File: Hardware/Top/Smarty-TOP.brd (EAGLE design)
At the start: 38 x 38 mm, 52 parts, among them SW6 SWITCH.MOM, SW7 SWITCH.MOM, SW8 SWITCH.MOM, U2 NRF52832_MODULE_MDBT42, U4 PCF8523

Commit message: Take 001 and part of Take 002 Completed
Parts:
- removed C10, C11: 300p, LinnesLab-Passives:C0603
- removed C12: 10u, LinnesLab-Passives:C0805
- removed C14: 100n, LinnesLab-Passives:C0603
- removed CORTEX1: CORTEX_DEBUG_PTH, LinnesLab-Connectors:2X5-PTH-1.27MM
- removed D1: (no value), LinnesLab-DiscreteSemi:USC
- removed L2: 10u, LinnesLab-Passives:L0603
- removed R8, R9: 10k, LinnesLab-Passives:R0603
- removed SW3, SW4: (no value), LinnesLab-Switches:BUTTON-GULLWING
- removed XTAL2: 32.768kHz, LinnesLab-Clocks:2-SMD.NOLEAD.2.0MMTO1.2MM
- added C26: 1u, LinnesLab-Passives:C0603
- added C27, C28: (no value), LinnesLab-Passives:C0603
- added C29, C30: 300p, LinnesLab-Passives:C0603
- added C31: 10u, LinnesLab-Passives:C0805
- added C32: 100n, LinnesLab-Passives:C0603
- added CORTEX3: CORTEX_DEBUG_PTH, LinnesLab-Connectors:2X5-PTH-1.27MM
- added D3: (no value), LinnesLab-DiscreteSemi:USC
- added JP2: (no value), LinnesLab-Switches:SMT-JUMPER_2_NO_SILK
- added L3: 10u, LinnesLab-Passives:L0603
- added LED5: RED, LinnesLab-LED:LED-0603
- added LED6: BLUE, LinnesLab-LED:LED-0603
- added R1, R2: 0, LinnesLab-Passives:R0603
- added R10: 27, LinnesLab-Passives:R0603
- added R16, R17, R19, R20: 1k, LinnesLab-Passives:R0603
- added R18: 10k, LinnesLab-Passives:R0603
- added SW1: SWITCH.MOM, LinnesLab-Switches:TACTILE_SWITCH_SMD_6.2MM_TALL
- added U5: NRF52832_MODULE_MDBT42, LinnesLab-Microcontrollers:BLE_MODULE_RAYTAC_MDBT42
- added XTAL4: 32.768kHz, LinnesLab-Clocks:2-SMD.NOLEAD.2.0MMTO1.2MM
- C7: value 1u -> 100n
- C8, C9: value (none) -> 47p
- LED4: value BLUE -> YELLOW
- R3, R4: value 1k -> 10k
- R5: value 10k -> 27
- SW7, SW8: value SWITCH.MOM -> (none); device LinnesLab-Switches:TACTILE_SWITCH_SMD_6.2MM_TALL -> LinnesLab-Switches:BUTTON-GULLWING
- U2: value NRF52832_MODULE_MDBT42 -> FT231XS; device LinnesLab-Microcontrollers:BLE_MODULE_RAYTAC_MDBT42 -> LinnesLab-DigitalIC:SSOP20_L
- moved SW7 59.6 mm to (75.1, 17.4)
- moved R4 58.9 mm to (-3.73, -11.9), turned to 0 degrees
- moved R3 55.4 mm to (-3.73, -9.22), turned to 0 degrees
- moved C7 42.3 mm to (65.6, 36.0), turned to 0 degrees
- moved C8 42.0 mm to (65.6, 30.9)
- moved SW8 38.7 mm to (68.0, 5.94), turned to 180 degrees
- moved C9 36.7 mm to (65.6, 25.9)
- moved XTAL3 32.6 mm to (7.70, -4.78)
- moved U4 32.4 mm to (12.4, -5.97)
- moved C2 32.1 mm to (14.2, -2.08)
- moved LED3 28.1 mm to (69.4, 35.8)
- moved LED4 26.2 mm to (69.4, 32.0)
- moved SW6 26.0 mm to (32.1, 4.04)
- moved R5 15.9 mm to (52.0, 33.8), turned to 0 degrees
- moved U2 14.0 mm to (18.4, 27.5), turned to 270 degrees
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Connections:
- net VBATT renamed VBAT
- removed net N$10: LED4.A, R4.1
- removed net N$18: SW6.B1, SW6.B2
- removed net N$21: SW7.A1, SW7.A2
- removed net N$22: SW7.B1, SW7.B2
- removed net N$23: SW8.A1, SW8.A2
- removed net N$24: SW8.B1, SW8.B2
- removed net N$4: C8.2, U2.13, XTAL2.P$1
- removed net N$6: C9.1, U2.14, XTAL2.P$2
- removed net N$9: LED3.A, R3.1
- removed net RXD: U2.21
- removed net TXD: U2.19
- new net !CTS: JP2.2, U2.9
- new net FT3V3: U2.13
- new net N$26: C27.2, U5.13, XTAL4.P$1
- new net N$27: C28.1, U5.14, XTAL4.P$2
- new net N$28: LED5.A, R16.1
- new net N$29: LED6.A, R17.1
- new net N$30: L3.1, U5.10
- new net N$31: C26.1, L3.2, U5.9
- new net N$32: CORTEX3.8
- new net RXD.FT: R2.1, U2.4
- new net RXD.NRF: R1.2, U5.21
- new net RXLED: R19.1, U2.17
- new net SW1: SW1.A1, SW6.A1
- new net TXD.FT: R1.1, U2.20
- new net TXD.NRF: R2.2, U5.19
- new net TXLED: R20.1, U2.10
- net 3.3V: now also C31.2, C7.2, CORTEX3.1, D3.-, LED3.A, LED4.A, R18.2, R3.2, R4.2, U2.14, U2.3, U5.11; no longer C12.2, CORTEX1.1, D1.-, R5.2, R8.2, R9.2, U2.11
- net DFU: now also SW7.3, U5.34; no longer SW3.3, U2.34
- net DTR: now also C32.1, U2.1; no longer C14.1
- net FRST: now also U5.38; no longer U2.38
- net GND: now also C26.2, C27.1, C28.2, C29.2, C30.2, C31.1, C7.1, C8.2, C9.1, CORTEX3.3, CORTEX3.5, CORTEX3.7, CORTEX3.9, JP2.1, LED5.C, LED6.C, SW1.B1, SW1.B2, SW6.B1, SW6.B2, SW7.1, SW8.3, U2.16, U2.6, U5.1, U5.12, U5.24, U5.39, USB2.S1, USB2.S2, USB2.S3, USB2.S4, USB2.S5, USB2.S6; no longer C10.2, C11.2, C12.1, C7.2, C8.1, C9.2, CORTEX1.3, CORTEX1.5, CORTEX1.7, CORTEX1.9, LED3.C, LED4.C, SW3.1, SW4.3, U2.1, U2.12, U2.24, U2.39
- net LED1: now also R16.2, U5.31; no longer R3.2, U2.31
- net LED2: now also R17.2, U5.33; no longer R4.2, U2.33
- net MISO: now also U5.28; no longer U2.28
- net MOSI: now also U5.27; no longer U2.27
- net N$11: now also R5.2, U2.12; no longer L2.1, U2.10
- net N$12: now also R10.2, U2.11; no longer C7.1, L2.2, U2.9
- net N$14: now also LED3.C, R19.2; no longer CORTEX1.8
- net N$16: now also LED4.C, R20.2; no longer SW6.A1, SW6.A2
- net P0.09/NFC1: now also C30.1, U5.22; no longer C11.1, U2.22
- net P0.10/NFC2: now also C29.1, U5.23; no longer C10.1, U2.23
- net RESET: now also C32.2, CORTEX3.10, D3.+, R18.1, SW8.1, U5.35; no longer C14.2, CORTEX1.10, D1.+, R5.1, SW4.1, U2.35
- net SCK: now also U5.26; no longer U2.26
- net SCL: now also R4.1, U5.3; no longer R8.1, U2.3
- net SDA: now also R3.1, U5.2; no longer R9.1, U2.2
- net SWCLK: now also CORTEX3.4, U5.36; no longer CORTEX1.4, U2.36
- net SWDIO: now also CORTEX3.2, U5.37; no longer CORTEX1.2, U2.37
- net SWO: now also CORTEX3.6, U5.32; no longer CORTEX1.6, U2.32
- net USB+: now also C8.1, R10.1
- net USB-: now also C9.2, R5.1
- net V_USB: now also U2.15

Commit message: Finished Take 2
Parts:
- removed SW6: SWITCH.MOM, LinnesLab-Switches:TACTILE_SWITCH_SMD_6.2MM_TALL
- added J1: (no value), LinnesLab-Connectors:1X07
- added SW2: SWITCH.MOM, LinnesLab-Switches:TACTILE_SWITCH_SMD_6.2MM_TALL
- moved SW1 10.3 mm to (32.1, 4.04)
- moved U2 0.90 mm to (19.1, 26.8)
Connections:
- removed net BATT: R13.1, R14.2
- removed net CD1: SD2.CD1
- removed net CHRG.STAT: CHRG2.1, R12.1
- removed net CS.OLED: U3.13
- removed net DC.OLED: U3.15
- removed net RESET.OLED: U3.14
- removed net SD.CS: SD2.2
- removed net SW1: SW1.A1, SW6.A1
- new net A4/BATT: R13.1, R14.2, U5.5
- new net A6/TIA: U5.7
- new net A7/PPG: U5.8
- new net D11/SW1: SW1.A1, U5.25
- new net D15/SW2: SW2.A1, U5.29
- new net D16/CS.OLED: U3.13, U5.30
- new net D27/CHRG.STATUS: CHRG2.1, R12.1, U5.4
- new net D29/LED.CTRL: U5.6
- new net D3/RESET.OLED: U3.14, U5.16
- new net D4/DC.OLED: U3.15, U5.17
- new net D5/CD1: SD2.CD1, U5.18
- new net D7/SD.CS: SD2.2, U5.20
- net GND: now also SW2.B1, SW2.B2; no longer SW6.B1, SW6.B2

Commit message: Finished Take 004
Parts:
- removed CHRG2: MCP73831, LinnesLab-Power:SOT23-5
- removed J1: (no value), LinnesLab-Connectors:1X07
- removed LDO2: MIC5504, LinnesLab-Power:SOT23-5
- removed R15: 100k, LinnesLab-Passives:R0603
- added CHRG: MCP73831, LinnesLab-Power:SOT23-5
- added J3: (no value), LinnesLab-Connectors:1X07_1.27MM
- added LDO1: MIC5504, LinnesLab-Power:SOT23-5
- moved R1 84.9 mm to (52.5, 60.1)
- moved R2 83.5 mm to (48.7, 59.9)
- moved U2 40.8 mm to (49.0, 54.6)
- moved R20 36.6 mm to (54.1, 57.6)
- moved C31 32.7 mm to (22.4, 26.3), turned to 270 degrees
- moved R19 31.8 mm to (54.0, 55.9)
- moved C26 30.7 mm to (25.0, 29.0), turned to 90 degrees
- moved C7 29.8 mm to (44.8, 57.5), turned to 270 degrees
- moved R7 28.4 mm to (30.7, 17.4)
- moved LED4 28.1 mm to (57.5, 57.5), turned to 180 degrees
- moved C20 28.1 mm to (18.1, -16.1), turned to 270 degrees
- moved R11 27.8 mm to (16.4, -15.9), turned to 90 degrees
- moved XTAL3 27.3 mm to (34.2, -11.3)
- moved L3 27.2 mm to (25.0, 25.8)
- moved C21 27.2 mm to (9.60, -16.3), turned to 180 degrees
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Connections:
- net 3.3V: now also J3.4, LDO1.5; no longer LDO2.5, R15.2
- net A6/TIA: now also J3.6
- net A7/PPG: now also J3.7
- net D27/CHRG.STATUS: now also CHRG.1; no longer CHRG2.1
- net D29/LED.CTRL: now also J3.5
- net GND: now also CHRG.2, J3.3, LDO1.2; no longer CHRG2.2, LDO2.2, R15.1, SW1.B2, SW2.B2
- net N$17: now also CHRG.5; no longer CHRG2.5
- net SCL: now also J3.2
- net SDA: now also J3.1
- net VIN: now also CHRG.4, LDO1.1, LDO1.3; no longer CHRG2.4, LDO2.1, LDO2.3
- net VLIPO: now also CHRG.3; no longer CHRG2.3
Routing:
- net GND: track 0.00 -> 20.5 mm, vias 0 -> 13
- net TXLED: track 0.00 -> 12.9 mm, vias 0 -> 2
- net VLIPO: track 0.00 -> 12.1 mm
- net VIN: track 0.00 -> 7.85 mm
- net N$2: track 0.00 -> 6.71 mm
- net RXD.FT: track 0.00 -> 5.63 mm
- net N$13: track 0.00 -> 5.40 mm
- net N$8: track 0.00 -> 4.43 mm
- net N$5: track 0.00 -> 4.30 mm
- net 3.3V: track 0.00 -> 3.99 mm, vias 0 -> 1
- net N$31: track 0.00 -> 3.96 mm
- net N$15: track 0.00 -> 3.32 mm
- net !CTS: track 0.00 -> 3.16 mm
- net N$3: track 0.00 -> 2.71 mm
- net N$1: track 0.00 -> 2.70 mm
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- added copper zone on layer 1, net 3.3V
- added copper zone on layer 16, net GND

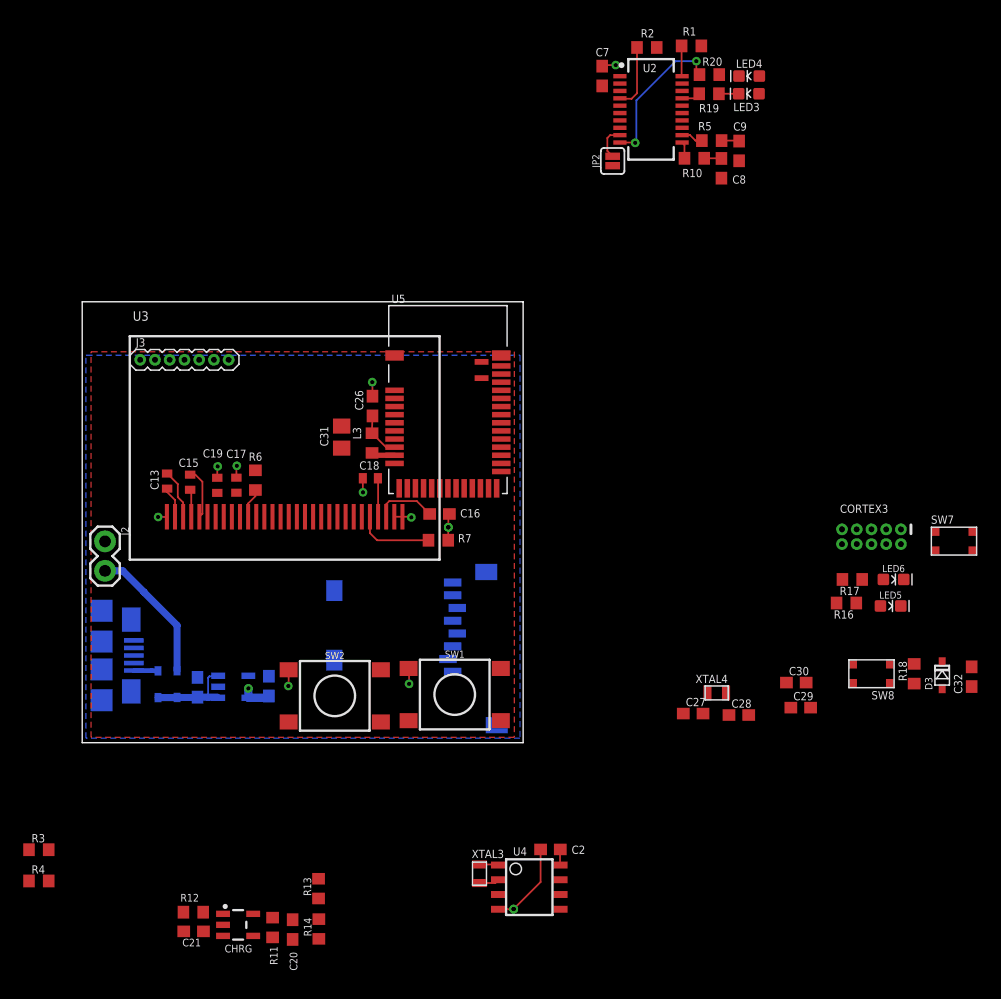
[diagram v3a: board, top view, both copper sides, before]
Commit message: Finished Take 005, Airwire Errors
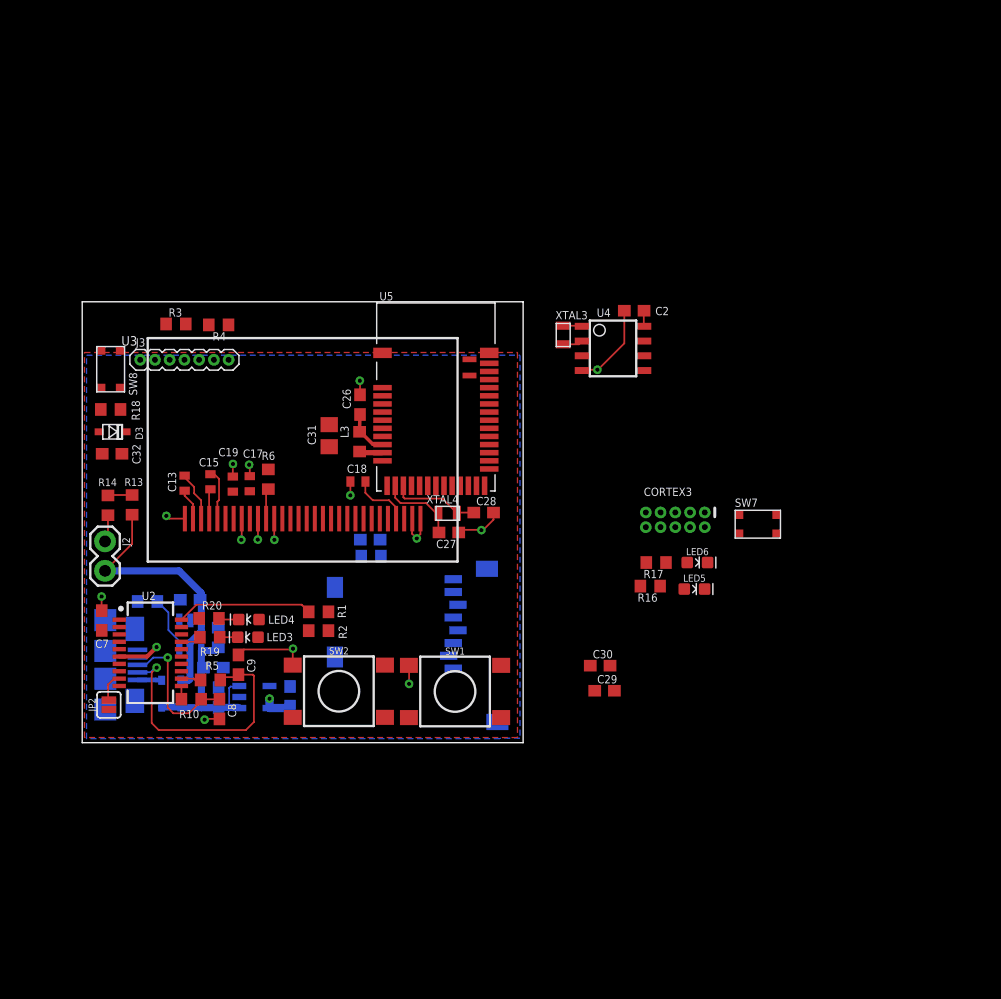
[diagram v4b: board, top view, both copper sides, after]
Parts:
- moved C32 76.5 mm to (2.57, 24.9), turned to 180 degrees
- moved D3 74.5 mm to (2.62, 26.8), turned to 0 degrees
- moved R18 72.9 mm to (2.45, 28.7), turned to 0 degrees
- moved SW8 70.6 mm to (2.45, 32.2), turned to 90 degrees
- moved JP2 63.9 mm to (2.30, 3.27)
- moved C7 63.7 mm to (1.69, 10.5)
- moved LED3 63.7 mm to (14.3, 9.09)
- moved R20 63.7 mm to (10.9, 10.7)
- moved U2 63.7 mm to (5.88, 7.75)
- moved R10 63.7 mm to (9.40, 3.74)
- moved LED4 63.7 mm to (14.4, 10.6)
- moved R19 63.6 mm to (11.0, 9.09)
- moved C8 63.6 mm to (11.8, 2.91)
- moved R5 63.5 mm to (11.0, 5.41)
- moved C9 61.8 mm to (13.5, 6.72), turned to 270 degrees
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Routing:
- net GND: track 20.5 -> 43.5 mm, vias 13 -> 16
- net USB-: track 1.61 -> 23.3 mm, vias 0 -> 1
- net TXLED: track 12.9 -> 0.39 mm, vias 2 -> 0
- net VLIPO: track 12.1 -> 23.6 mm
- net USB+: track 1.49 -> 12.5 mm, vias 0 -> 1
- net TXD.FT: track 2.63 -> 11.8 mm
- net VIN: track 7.85 -> 15.9 mm
- net N$27: track 0.00 -> 7.67 mm
- net N$26: track 0.00 -> 6.98 mm
- net N$2: track 6.71 -> 0.00 mm
- net RXD.FT: track 5.63 -> 0.05 mm
- net N$13: track 5.40 -> 0.00 mm
- net N$17: track 0.00 -> 5.01 mm
- net A4/BATT: track 0.00 -> 2.10 mm
- net N$15: track 3.32 -> 5.15 mm
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
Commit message: Finished Take 006
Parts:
- removed C2, C5, C6: 1u, LinnesLab-Passives:C0603
- removed C20, C21: 4.7u, LinnesLab-Passives:C0603
- removed CHRG: MCP73831, LinnesLab-Power:SOT23-5
- removed LDO1: MIC5504, LinnesLab-Power:SOT23-5
- removed R11: (no value), LinnesLab-Passives:R0603
- removed R12: 100k, LinnesLab-Passives:R0603
- removed SD2: (no value), LinnesLab-Connectors:MICROSD
- removed U4: PCF8523, LinnesLab-Clocks:SO8
- removed XTAL3: 32.7680kHz, LinnesLab-Clocks:2-SMD.NOLEAD.2.0MMTO1.2MM
- moved R18 36.3 mm to (35.0, 12.8), turned to 180 degrees
- moved SW8 36.1 mm to (34.7, 15.9), turned to 270 degrees
- moved C32 36.0 mm to (35.0, 9.38), turned to 0 degrees
- moved D3 35.9 mm to (34.9, 11.1), turned to 180 degrees
- moved SW7 28.7 mm to (35.0, 35.8)
- moved LED5 20.7 mm to (33.5, 20.8), turned to 270 degrees
- moved CORTEX3 19.0 mm to (35.2, 29.5), turned to 270 degrees
- moved R16 18.6 mm to (33.7, 24.0), turned to 90 degrees
- moved LED6 18.3 mm to (35.5, 20.8), turned to 270 degrees
- moved C18 17.2 mm to (41.0, 22.3)
- moved R17 16.4 mm to (35.4, 24.0), turned to 90 degrees
- moved C28 16.1 mm to (18.8, 22.5), turned to 90 degrees
- moved C27 15.1 mm to (17.2, 22.5), turned to 270 degrees
- moved XTAL4 11.3 mm to (20.5, 22.1), turned to 90 degrees
- moved R7 7.55 mm to (31.8, 19.2), flipped to the top, turned to 270 degrees
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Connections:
- removed net CD2: SD2.CD2
- removed net N$17: CHRG.5, R11.2
- removed net N$19: U4.2, XTAL3.P$1
- removed net N$20: U4.1, XTAL3.P$2
- removed net VBAT: U4.3
- net 3.3V: no longer C2.1, C6.1, LDO1.5, SD2.4, U4.8
- net D27/CHRG.STATUS: no longer CHRG.1, R12.1
- net D5/CD1: no longer SD2.CD1
- net D7/SD.CS: no longer SD2.2
- net GND: no longer C2.2, C20.2, C21.1, C5.1, C6.2, CHRG.2, LDO1.2, R11.1, SD2.6, SD2.MT1, SD2.MT2, U4.4
- net MISO: no longer SD2.7
- net MOSI: no longer SD2.3
- net SCK: no longer SD2.5
- net SCL: no longer U4.6
- net SDA: no longer U4.5
- net VIN: no longer C21.2, C5.2, CHRG.4, LDO1.1, LDO1.3, R12.2
- net VLIPO: no longer C20.1, CHRG.3
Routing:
- net RESET: track 0.00 -> 28.5 mm, vias 0 -> 1
- net VIN: track 15.9 -> 1.76 mm
- net SWO: track 0.00 -> 12.0 mm, vias 0 -> 1
- net SWCLK: track 0.00 -> 8.34 mm
- net N$2: track 0.00 -> 7.78 mm
- net LED2: track 0.00 -> 7.66 mm
- net SWDIO: track 0.00 -> 5.53 mm, vias 0 -> 1
- net N$15: track 5.15 -> 0.05 mm
- net N$17: track 5.01 -> 0.00 mm
- net GND: track 43.5 -> 39.0 mm, vias 16 -> 19
- net LED1: track 0.00 -> 4.33 mm
- net N$13: track 0.00 -> 4.27 mm
- net 3.3V: track 3.99 -> 0.11 mm, vias 1 -> 0
- net VLIPO: track 23.6 -> 20.7 mm
- net N$19: track 1.76 -> 0.00 mm
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
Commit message: Almost Done With Take 008
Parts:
- removed C19: 2.2uF, LinnesLab-Passives:C0402
- removed C26: 1u, LinnesLab-Passives:C0603
- removed C27, C28: (no value), LinnesLab-Passives:C0603
- removed C29, C30: 300p, LinnesLab-Passives:C0603
- removed C31: 10u, LinnesLab-Passives:C0805
- removed CORTEX3: CORTEX_DEBUG_PTH, LinnesLab-Connectors:2X5-PTH-1.27MM
- removed L3: 10u, LinnesLab-Passives:L0603
- removed LED5: RED, LinnesLab-LED:LED-0603
- removed LED6: BLUE, LinnesLab-LED:LED-0603
- removed R19, R20: 1k, LinnesLab-Passives:R0603
- removed SW7: (no value), LinnesLab-Switches:BUTTON-GULLWING
- removed XTAL4: 32.768kHz, LinnesLab-Clocks:2-SMD.NOLEAD.2.0MMTO1.2MM
- added C1, C6: 1u, LinnesLab-Passives:C0603
- added C11: 47p, LinnesLab-Passives:C0603
- added C12: 100n, LinnesLab-Passives:C0603
- added C14: 2.2uF, LinnesLab-Passives:C0402
- added C2: 10u, LinnesLab-Passives:C0805
- added C3, C4: (no value), LinnesLab-Passives:C0603
- added C5: 4.7u, LinnesLab-Passives:C0603
- added CHRG1: MCP73831, LinnesLab-Power:SOT23-5
- added DEBUG1: CORTEX_DEBUG_PTH, LinnesLab-Connectors:2X5-PTH-1.27MM
- added L1: 10u, LinnesLab-Passives:L0603
- added LDO1: MIC5504, LinnesLab-Power:SOT23-5
- added LED1: RED, LinnesLab-LED:LED-0603
- added LED2: BLUE, LinnesLab-LED:LED-0603
- added R11: 27, LinnesLab-Passives:R0603
- added R12: 10k, LinnesLab-Passives:R0603
- added R15: 1k, LinnesLab-Passives:R0603
- added R8: 100k, LinnesLab-Passives:R0603
- added SW3: SWITCH.MOM, LinnesLab-Switches:TACTILE_SWITCH_SMD_6.2MM_TALL
- added XTAL1: 32.768kHz, LinnesLab-Clocks:2-SMD.NOLEAD.2.0MMTO1.2MM
- C13: value 2.2uF -> 10uF; device LinnesLab-Passives:C0402 -> LinnesLab-Passives:C0603
- C15: device LinnesLab-Passives:C0402 -> LinnesLab-Passives:C0603
- C16: value 10uF -> 2.2uF; device LinnesLab-Passives:C0603 -> LinnesLab-Passives:C0402
- C7: value 100n -> 1u
- C8: value 47p -> 4.7u
- R1, R2: value 0 -> 10k
- R13: value 100k -> 390k
- R14: value 100k -> 1k
- R16, R17: value 1k -> 0
- R3: value 10k -> 100k
- R4: value 10k -> 1k
- R5: value 27 -> 1k
- R6: value 10k -> (none)
- R7: value 390k -> 100k
- SW2: value SWITCH.MOM -> (none); device LinnesLab-Switches:TACTILE_SWITCH_SMD_6.2MM_TALL -> LinnesLab-Switches:BUTTON-GULLWING
- moved SW2 33.9 mm to (34.9, 35.7)
- moved R5 30.8 mm to (35.7, 23.9), turned to 90 degrees
- moved R2 29.6 mm to (3.18, 33.7), turned to 90 degrees
- moved R1 29.3 mm to (1.60, 33.8), turned to 90 degrees
- moved R7 27.5 mm to (4.30, 20.5)
- moved R13 27.2 mm to (31.4, 19.1)
- moved C18 27.1 mm to (13.9, 22.4), turned to 270 degrees
- moved R4 25.3 mm to (34.0, 23.9), turned to 90 degrees
- moved C8 23.2 mm to (2.83, 24.2), turned to 180 degrees
- moved C13 21.9 mm to (29.9, 19.1), turned to 90 degrees
- moved C16 21.7 mm to (8.71, 22.3), turned to 270 degrees
- moved C7 20.8 mm to (11.5, 28.9), turned to 180 degrees
- moved R16 20.4 mm to (20.0, 8.91), turned to 0 degrees
- moved R17 20.1 mm to (19.8, 11.3), turned to 0 degrees
- moved C15 19.6 mm to (28.3, 14.7), turned to 180 degrees
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- renumbered C32 to C10, D4 to D1, D5 to D2, J3 to J1, JP2 to JP1, R18 to R9, SW8 to RESET, U5 to U1, USB2 to USB1
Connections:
- removed net A4/BATT: R13.1, R14.2, U1.5
- removed net A6/TIA: J1.6, U1.7
- removed net A7/PPG: J1.7, U1.8
- removed net D29/LED.CTRL: J1.5, U1.6
- new net A4/PPG: J1.7, U1.5
- new net A5/TIA: J1.6, U1.6
- new net A7/BATT: R7.1, R8.2, U1.8
- new net D30/LED.CTRL: J1.5, U1.7
- new net N$4: CHRG1.5, R6.2
- net 3.3V: now also C12.2, C18.2, C2.2, C7.1, DEBUG1.1, LDO1.5, R1.2, R2.2; no longer C19.2, C31.2, C7.2, CORTEX3.1, R3.2, R4.2
- net D15/SW2: now also SW3.A1; no longer SW2.A1
- net D27/CHRG.STATUS: now also CHRG1.1, R3.1
- net DFU: now also SW2.3; no longer SW7.3
- net GND: now also C1.2, C11.2, C12.1, C13.1, C15.1, C2.1, C3.1, C4.2, C5.1, C6.1, C7.2, CHRG1.2, DEBUG1.3, DEBUG1.5, DEBUG1.7, DEBUG1.9, LDO1.2, LED1.C, LED2.C, R12.1, R13.2, R8.1, SW2.1, SW3.B1; no longer C16.1, C19.1, C26.2, C27.1, C28.2, C29.2, C30.2, C31.1, C7.1, CORTEX3.3, CORTEX3.5, CORTEX3.7, CORTEX3.9, LED5.C, LED6.C, R14.1, R7.2, SW2.B1, SW7.1
- net LED1: now also R4.2; no longer R16.2
- net LED2: now also R5.2; no longer R17.2
- net N$1: now also R12.2; no longer R6.2
- net N$11: now also R10.2; no longer R5.2
- net N$12: now also R11.2; no longer R10.2
- net N$13: now also C13.2; no longer C16.2
- net N$14: now also R14.2; no longer R19.2
- net N$15: now also C15.2; no longer C18.2
- net N$16: now also R15.2; no longer R20.2
- net N$2: now also R13.1; no longer R7.1
- net N$26: now also C3.2, XTAL1.P$1; no longer C27.2, XTAL4.P$1
- net N$27: now also C4.1, XTAL1.P$2; no longer C28.1, XTAL4.P$2
- net N$28: now also LED1.A, R4.1; no longer LED5.A, R16.1
- net N$29: now also LED2.A, R5.1; no longer LED6.A, R17.1
- net N$3: now also C16.2; no longer C13.2
- net N$30: now also L1.1; no longer L3.1
- net N$31: now also C1.1, L1.2; no longer C26.1, L3.2
- net N$32: now also DEBUG1.8; no longer CORTEX3.8
- net N$5: now also C16.1; no longer C13.1
- net N$7: now also C14.2; no longer C15.2
- net N$8: now also C14.1; no longer C15.1
- net P0.09/NFC1: no longer C30.1
- net P0.10/NFC2: no longer C29.1
- net RESET: now also DEBUG1.10; no longer CORTEX3.10
- net RXD.FT: now also R17.1; no longer R2.1
- net RXD.NRF: now also R16.2; no longer R1.2
- net RXLED: now also R14.1; no longer R19.1
- net SCL: now also R2.1; no longer R4.1
- net SDA: now also R1.1; no longer R3.1
- net SWCLK: now also DEBUG1.4; no longer CORTEX3.4
- net SWDIO: now also DEBUG1.2; no longer CORTEX3.2
- net SWO: now also DEBUG1.6; no longer CORTEX3.6
- net TXD.FT: now also R16.1; no longer R1.1
- net TXD.NRF: now also R17.2; no longer R2.2
- net TXLED: now also R15.1; no longer R20.1
- net USB+: now also C11.1, R11.1; no longer C8.1, R10.1
- net USB-: now also R10.1; no longer R5.1
- net VIN: now also C5.2, C6.2, CHRG1.4, LDO1.1, LDO1.3, R3.2
- net VLIPO: now also C8.1, CHRG1.3, R7.2; no longer R13.2
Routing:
- net VIN: track 1.76 -> 46.9 mm, vias 0 -> 1
- net DTR: track 0.00 -> 33.7 mm, vias 0 -> 2
- net D27/CHRG.STATUS: track 0.00 -> 27.7 mm, vias 0 -> 4
- net GND: track 39.0 -> 65.7 mm, vias 19 -> 28
- net RXD.NRF: track 0.00 -> 26.2 mm, vias 0 -> 2
- net SDA: track 0.00 -> 24.1 mm, vias 0 -> 1
- net D15/SW2: track 0.00 -> 23.9 mm, vias 0 -> 2
- net A7/BATT: track 0.00 -> 23.3 mm, vias 0 -> 2
- net SCL: track 0.00 -> 22.8 mm, vias 0 -> 1
- net TXD.NRF: track 0.00 -> 22.1 mm, vias 0 -> 2
- net D11/SW1: track 0.00 -> 20.2 mm
- net D16/CS.OLED: track 0.00 -> 18.6 mm, vias 0 -> 2
- net RXD.FT: track 0.05 -> 17.7 mm
- net SCK: track 0.00 -> 17.1 mm, vias 0 -> 2
- net MOSI: track 0.00 -> 15.1 mm, vias 0 -> 2
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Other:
- board text added: "+"
